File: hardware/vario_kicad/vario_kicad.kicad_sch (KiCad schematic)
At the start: 58 parts, among them P1 USB_C_Plug_USB2.0, U2 BME280, U3 W25Q128JVS, U4 STM32L072CBTx

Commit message: updates;
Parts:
- added Q1: PMOS, symbol Simulation_SPICE:PMOS
- added Q2: NMOS, symbol Simulation_SPICE:NMOS
- added R25: 22k, symbol Device:R
- added R26, R27: 100k, symbol Device:R
- BT1: footprint (none) -> symbol_lib:lipo_footprint; now not fitted
- R22: value 10mR -> 10k
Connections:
- net AUDIO_AMP_ENABLE: now also R16.1; no longer R16.2
- net GND: now also BT1.2 (-), R16.2, Q2.3 (S), R25.2, R27.2; no longer R22.2
- net VBATT: now also Q1.3 (S), R26.2; no longer R16.1
- net ADC_IN3: now reaches U4.13 (PA3)
- net ADC_IN3: now also R22.2, R25.1
- net BP_DIVIDER_ENABLE: now reaches U4.39 (PB3)
- net BP_DIVIDER_ENABLE: now also Q2.2 (G), R27.1
- net VBATT_SW: now reaches R22.1
- net VBATT_SW: now also Q1.1 (D); no longer BT1.2 (-)
- new net: Q1.2 (G), Q2.1 (D), R26.1
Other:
- note added: "#TODO add 3 push buttons"
- note added: "#TODO should it be vbatt or vbatt_sw"
- note added: "Battery charge and regulator"
- note added: "Battery level measuring circuit"
- note added: "I_charge = 100mA"
- note added: "Max V_BATT voltage 4.3V max adc voltage 2.95V"
- note added: "audio amp disabled by default"
- note added: "~0.1uA in sleep mode"
- note added: "~1uA in power-down"
- note removed: "TODO add a current sense amplifier"
- moved on the sheet: C11, C12, C13, D4, R23, R24, TP7, TP8, U5, U6

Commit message: add push button switches
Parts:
- added J1: ~, symbol_lib:SWD_programming, symbol New_Library:SWD_PROGRAMMING
- R22: value 10k -> 100k
- R25: value 22k -> 220k
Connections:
- net GND: now also J1.4 (GND)
- net MEM_CS_ALT: now also U4.40 (PB4); no longer U4.12 (PA2)
- net SWCLK: now also J1.3 (SWD_CLK)
- net SWDIO: now also J1.2 (SWD_TDIO)
- net VBATT: no longer C5.1, C9.1, U1.6 (VCC)
- net VBATT_SW: now also C5.1, C9.1, U1.6 (VCC)
- net VCC: now also J1.1 (3V3)
- net SW1: now reaches U4.41 (PB5)
- net SW3: now reaches U4.42 (PB6)
- net BP_DIVIDER_ENABLE renamed VBATT_SW_EN
- net TIM2_CH1 renamed TIM2_CH3
- net TIM2_CH3: now also U4.12 (PA2); no longer U4.10 (PA0)
- new net WKUP1: U4.10 (PA0)
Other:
- added sheet switch1 (myswitch.kicad_sch)
- added sheet switch2 (myswitch.kicad_sch)
- added sheet switch3 (myswitch.kicad_sch)
- note removed: "#TODO add 3 push buttons"
- note removed: "#TODO should it be vbatt or vbatt_sw"
- note removed: "Battery level measuring circuit"

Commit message: minor updates
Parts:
- removed L1: 10uH, symbol Device:L
- removed U6: ~, Package_TO_SOT_SMD:SOT-23, symbol New_Library:____XC6206P332MR-G
- added U6: ~, Package_TO_SOT_SMD:SOT-23, symbol New_Library:XC6206P332MR-G
- BT1: now fitted
- C10: value 1uF -> 10nF
- R21: value 330R -> 680R
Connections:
- net AUDIO_AMP_ENABLE: now also R16.2; no longer R16.1
- net GND: now also U6.1 (VSS); no longer R16.2
- net VBATT: now also U6.2 (VOUT)
- net VBATT_SW: now also R16.1
- net VCC: now also U6.2 (VOUT)
- net at R21.1: now also C10.1, R20.2
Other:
- note added: "audio amp enabled by default"
- note added: "f_cutoff = 23.4 kHz"
- note removed: "audio amp disabled by default"
- moved on the sheet: R21

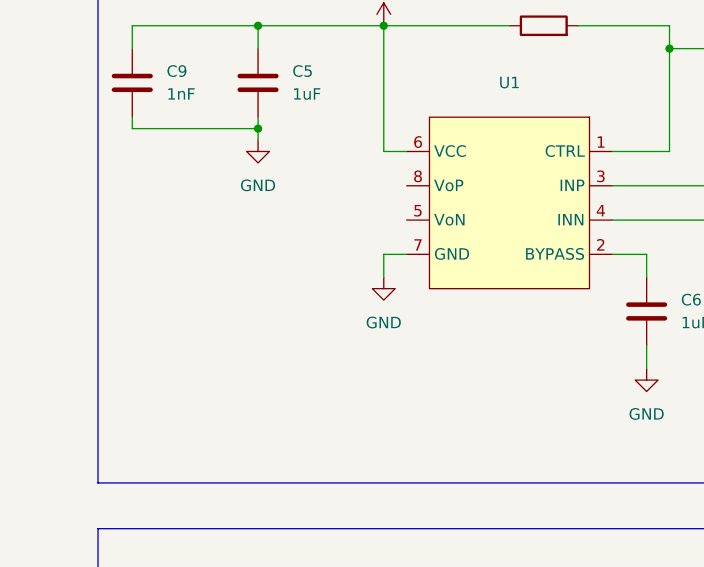
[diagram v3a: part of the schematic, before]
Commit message: update some component footprints
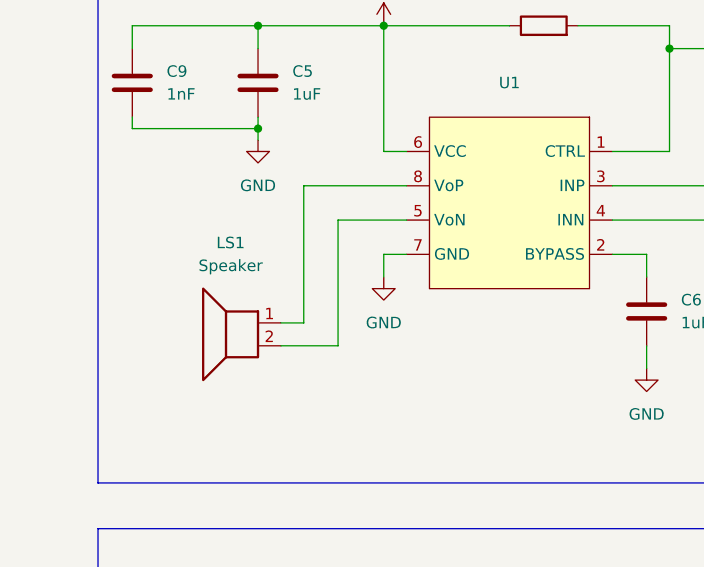
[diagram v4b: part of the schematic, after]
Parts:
- added LS1: Speaker, symbol_lib:speaker_footprint, symbol Device:Speaker
- C1, C10, C11, C12, C13, C2, C3, C4, C5, C6, C7, C8, C9: footprint (none) -> Capacitor_SMD:C_0603_1608Metric
- D1, D2, D3, D4: footprint (none) -> LED_SMD:LED_0603_1608Metric_Pad1.05x0.95mm_HandSolder
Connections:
- net at U1.5 (VoN): now also LS1.2
- net at U1.8 (VoP): now also LS1.1
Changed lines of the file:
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@@
 	(wire
 		(pts
+			(xy 45.72 176.53) (xy 57.15 176.53)
+		)
+		(stroke
+			(width 0)
+			(type default)
+		)
+	)
+	(wire
+		(pts
 			(xy 40.64 135.89) (xy 67.31 135.89)
 		)
@@
 	(wire
 		(pts
+			(xy 57.15 180.34) (xy 49.53 180.34)
+		)
+		(stroke
+			(width 0)
+			(type default)
+		)
+	)
+	(wire
+		(pts
 			(xy 90.17 41.91) (xy 90.17 46.99)
 		)
@@
 	(wire
 		(pts
+			(xy 49.53 180.34) (xy 49.53 194.31)
+		)
+		(stroke
+			(width 0)
+			(type default)
+		)
+	)
+	(wire
+		(pts
 			(xy 45.72 26.67) (xy 45.72 29.21)
 		)
@@
 	(wire
 		(pts
+			(xy 49.53 194.31) (xy 43.18 194.31)
+		)
+		(stroke
+			(width 0)
+			(type default)
+		)
+	)
+	(wire
+		(pts
 			(xy 40.64 168.91) (xy 40.64 170.18)
 		)
@@
 	(wire
 		(pts
+			(xy 45.72 191.77) (xy 45.72 176.53)
+		)
+		(stroke
+			(width 0)
+			(type default)
+		)
+	)
+	(wire
+		(pts
 			(xy 388.62 236.22) (xy 388.62 238.76)
 		)
@@
 	(wire
 		(pts
+			(xy 43.18 191.77) (xy 45.72 191.77)
+		)
+		(stroke
+			(width 0)
+			(type default)
+		)
+	)
+	(wire
+		(pts
 			(xy 254 133.35) (xy 265.43 133.35)
 		)
@@
 			)
 		)
-		(property "Footprint" ""
+		(property "Footprint" "LED_SMD:LED_0603_1608Metric_Pad1.05x0.95mm_HandSolder"
 			(at 373.38 220.98 0)
 			(effects
@@
 			)
 		)
-		(property "Footprint" ""
+		(property "Footprint" "LED_SMD:LED_0603_1608Metric_Pad1.05x0.95mm_HandSolder"
 			(at 388.62 220.98 0)
 			(effects
@@
 			)
 		)
-		(property "Footprint" ""
+		(property "Footprint" "Capacitor_SMD:C_0603_1608Metric"
 			(at 27.6352 168.91 0)
 			(effects
@@
 			)
 		)
-		(property "Footprint" ""
+		(property "Footprint" "Capacitor_SMD:C_0603_1608Metric"
 			(at 274.0152 238.76 0)
 			(effects
@@
 			)
 		)
-		(property "Footprint" ""
+		(property "Footprint" "Capacitor_SMD:C_0603_1608Metric"
 			(at 41.6052 168.91 0)
 			(effects
@@
 			)
 		)
-		(property "Footprint" ""
+		(property "Footprint" "Capacitor_SMD:C_0603_1608Metric"
 			(at 219.4052 113.03 0)
 			(effects
@@
 			)
 		)
-		(property "Footprint" ""
+		(property "Footprint" "Capacitor_SMD:C_0603_1608Metric"
 			(at 36.5252 236.22 0)
 			(effects
@@
 			)
 		)
-		(property "Footprint" ""
+		(property "Footprint" "Capacitor_SMD:C_0603_1608Metric"
 			(at 121.6152 57.15 0)
 			(effects
@@
 			)
 		)
-		(property "Footprint" ""
+		(property "Footprint" "LED_SMD:LED_0603_1608Metric_Pad1.05x0.95mm_HandSolder"
 			(at 356.87 220.98 0)
 			(effects
@@
 			)
 		)
-		(property "Footprint" ""
+		(property "Footprint" "Capacitor_SMD:C_0603_1608Metric"
 			(at 21.2852 38.1 0)
 			(effects
@@
 			)
 		)
-		(property "Datasheet" "https://ngspice.sourceforge.io/docs/ngspice-html-manual/manual.xhtml#cha_MOSFETs"
+		(property "Datasheet" ""
 			(at 46.99 91.44 0)
 			(effects
@@
 			)
 		)
-		(property "Datasheet" "https://www.usb.org/sites/default/files/documents/usb_type-c.zip"
+		(property "Datasheet" ""
 			(at 383.54 133.35 0)
 			(effects
@@
 			)
 		)
-		(property "Footprint" ""
+		(property "Footprint" "Capacitor_SMD:C_0603_1608Metric"
 			(at 50.4952 236.22 0)
 			(effects
@@
 			)
 		)
-		(property "Footprint" ""
+		(property "Footprint" "Capacitor_SMD:C_0603_1608Metric"
 			(at 142.24 184.4548 0)
 			(effects
@@
 			)
 		)
-		(property "Footprint" ""
+		(property "Footprint" "Capacitor_SMD:C_0603_1608Metric"
 			(at 168.6052 189.23 0)
 			(effects
@@
 			)
 		)
-		(property "Footprint" ""
+		(property "Footprint" "Capacitor_SMD:C_0603_1608Metric"
 			(at 142.24 170.4848 0)
 			(effects
@@
 			)
 		)
-		(property "Datasheet" "https://ngspice.sourceforge.io/docs/ngspice-html-manual/manual.xhtml#cha_MOSFETs"
+		(property "Datasheet" ""
 			(at 31.75 133.35 0)
 			(effects
@@
 			)
 		)
-		(property "Footprint" ""
+		(property "Footprint" "LED_SMD:LED_0603_1608Metric_Pad1.05x0.95mm_HandSolder"
 			(at 33.02 39.37 0)
 			(effects
@@
 			)
 		)
-		(property "Footprint" ""
+		(property "Footprint" "Capacitor_SMD:C_0603_1608Metric"
 			(at 167.3352 57.15 0)
 			(effects
@@
 	)
 	(symbol
+		(lib_id "Device:Speaker")
+		(at 38.1 191.77 0)
+		(mirror y)
+		(unit 1)
+		(exclude_from_sim no)
+		(in_bom yes)
+		(on_board yes)
+		(dnp no)
+		(fields_autoplaced yes)
+		(property "Reference" "LS1"
+			(at 37.592 182.88 0)
+			(effects
+				(font
+					(size 1.27 1.27)
+				)
+			)
+		)
+		(property "Value" "Speaker"
+			(at 37.592 185.42 0)
+			(effects
+				(font
+					(size 1.27 1.27)
+				)
+			)
+		)
+		(property "Footprint" "symbol_lib:speaker_footprint"
+			(at 38.1 196.85 0)
+			(effects
+				(font
+					(size 1.27 1.27)
+				)
+				(hide yes)
+			)
+		)
+		(property "Datasheet" "https://www.lcsc.com/product-detail/Speakers_INGHAi-GSPK2307P-8R1W_C530531.html"
+			(at 38.354 193.04 0)
+			(effects
+				(font
+					(size 1.27 1.27)
+				)
+				(hide yes)
+			)
+		)
+		(property "Description" "Speaker"
+			(at 38.1 191.77 0)
+			(effects
+				(font
+					(size 1.27 1.27)
+				)
+				(hide yes)
+			)
+		)
+		(pin "1"
+		)
+		(pin "2"
+		)
+		(instances
+			(project ""
+				(path "/50389aff-b244-451e-8e3a-c5addd2215e1"
+					(reference "LS1")
+					(unit 1)
+				)
+			)
+		)
+	)
+	(symbol
 		(lib_id "Device:R")
 		(at 72.39 158.75 90)
@@
 			)
 		)
-		(property "Footprint" ""
+		(property "Footprint" "Capacitor_SMD:C_0603_1608Metric"
 			(at 84.7852 194.31 0)
 			(effects

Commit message: move external components to separate sheets
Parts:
- removed BT1: Battery_Cell, symbol_lib:lipo_footprint, symbol Device:Battery_Cell
- removed C1, C2, C3, C7, C8: 100nF, Capacitor_SMD:C_0603_1608Metric, symbol Device:C
- removed C10: 10nF, Capacitor_SMD:C_0603_1608Metric, symbol Device:C
- removed C11, C12, C13, C5, C6: 1uF, Capacitor_SMD:C_0603_1608Metric, symbol Device:C
- removed C9: 1nF, Capacitor_SMD:C_0603_1608Metric, symbol Device:C
- removed D1, D2, D3, D4: LED, LED_SMD:LED_0603_1608Metric_Pad1.05x0.95mm_HandSolder, symbol Device:LED
- removed LS1: Speaker, symbol_lib:speaker_footprint, symbol Device:Speaker
- removed Q1: PMOS, symbol Simulation_SPICE:PMOS
- removed Q2: NMOS, symbol Simulation_SPICE:NMOS
- removed R1, R2: 4k7, symbol Device:R
- removed R10, R11, R24, R3: 10k, symbol Device:R
- removed R12, R13, R14: 1k, symbol Device:R
- removed R16, R17, R18, R22, R26, R27: 100k, symbol Device:R
- removed R19, R20, R5, R6, R7, R8, R9: 0R, symbol Device:R
- removed R21: 680R, symbol Device:R
- removed R23: 330R, symbol Device:R
- removed R25: 220k, symbol Device:R
- removed TP1, TP2: ~, symbol Connector:TestPoint
- removed TP7, TP8: TestPoint, symbol Connector:TestPoint
- removed U1: ~, Package_SO:MSOP-8-1EP_3x3mm_P0.65mm_EP1.73x1.85mm, symbol New_Library:NS4150B
- removed U2: BME280, Package_LGA:Bosch_LGA-8_2.5x2.5mm_P0.65mm_ClockwisePinNumbering, symbol Sensor:BME280
- removed U3: W25Q128JVS, Package_SO:SOIC-8_5.23x5.23mm_P1.27mm, symbol Memory_Flash:W25Q128JVS
- removed U5: ~, Package_TO_SOT_SMD:SOT-23-5, symbol New_Library:TP4054
- removed U6: ~, Package_TO_SOT_SMD:SOT-23, symbol New_Library:XC6206P332MR-G
- P1: footprint (none) -> symbol_lib:my_usbc
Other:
- added sheet audio_amp (audio_amp.kicad_sch)
- added sheet bme280 (bme280.kicad_sch)
- added sheet leds (leds.kicad_sch)
- added sheet memory (memory.kicad_sch)
- added sheet power (power.kicad_sch)
- note removed: "Battery charge and regulator"
- note removed: "I_charge = 100mA"
- note removed: "Max V_BATT voltage 4.3V max adc voltage 2.95V"
- note removed: "SDO = high => i2c address = 0x77"
- note removed: "audio amp enabled by default"
- note removed: "f_cutoff = 23.4 kHz"
- note removed: "gain settings resistors"
- note removed: "~0.1uA in sleep mode"
- note removed: "~1uA in power-down"
- moved on the sheet: C4, J1, P1, R15, R4, TP3, TP4, TP5, TP6, U4

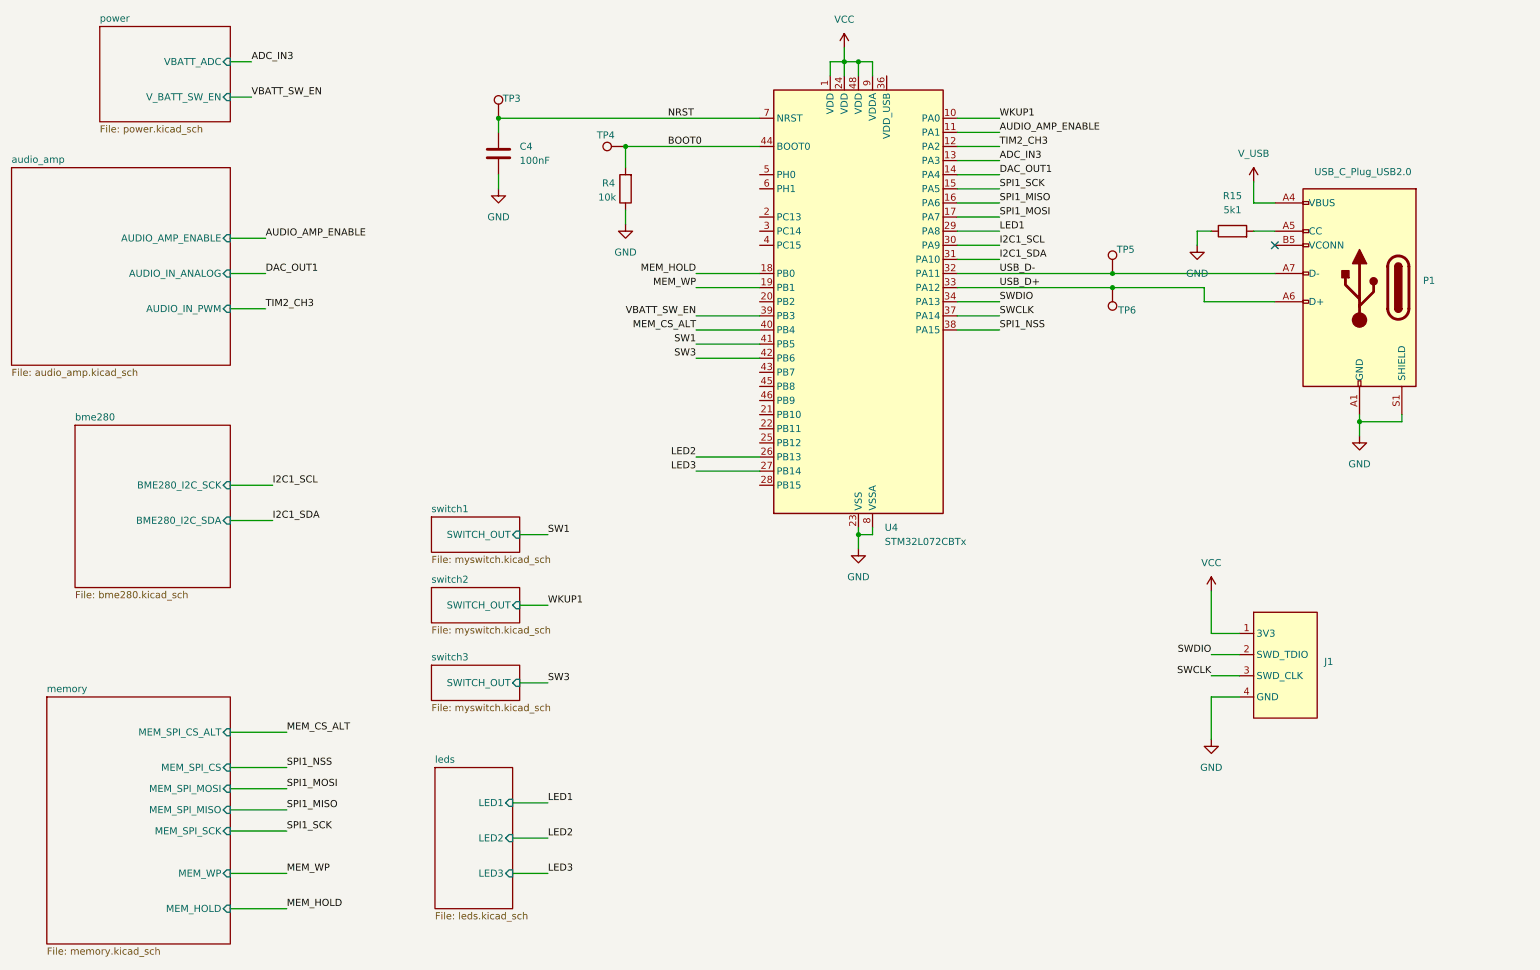
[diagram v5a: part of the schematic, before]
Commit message: all components in hier sheets
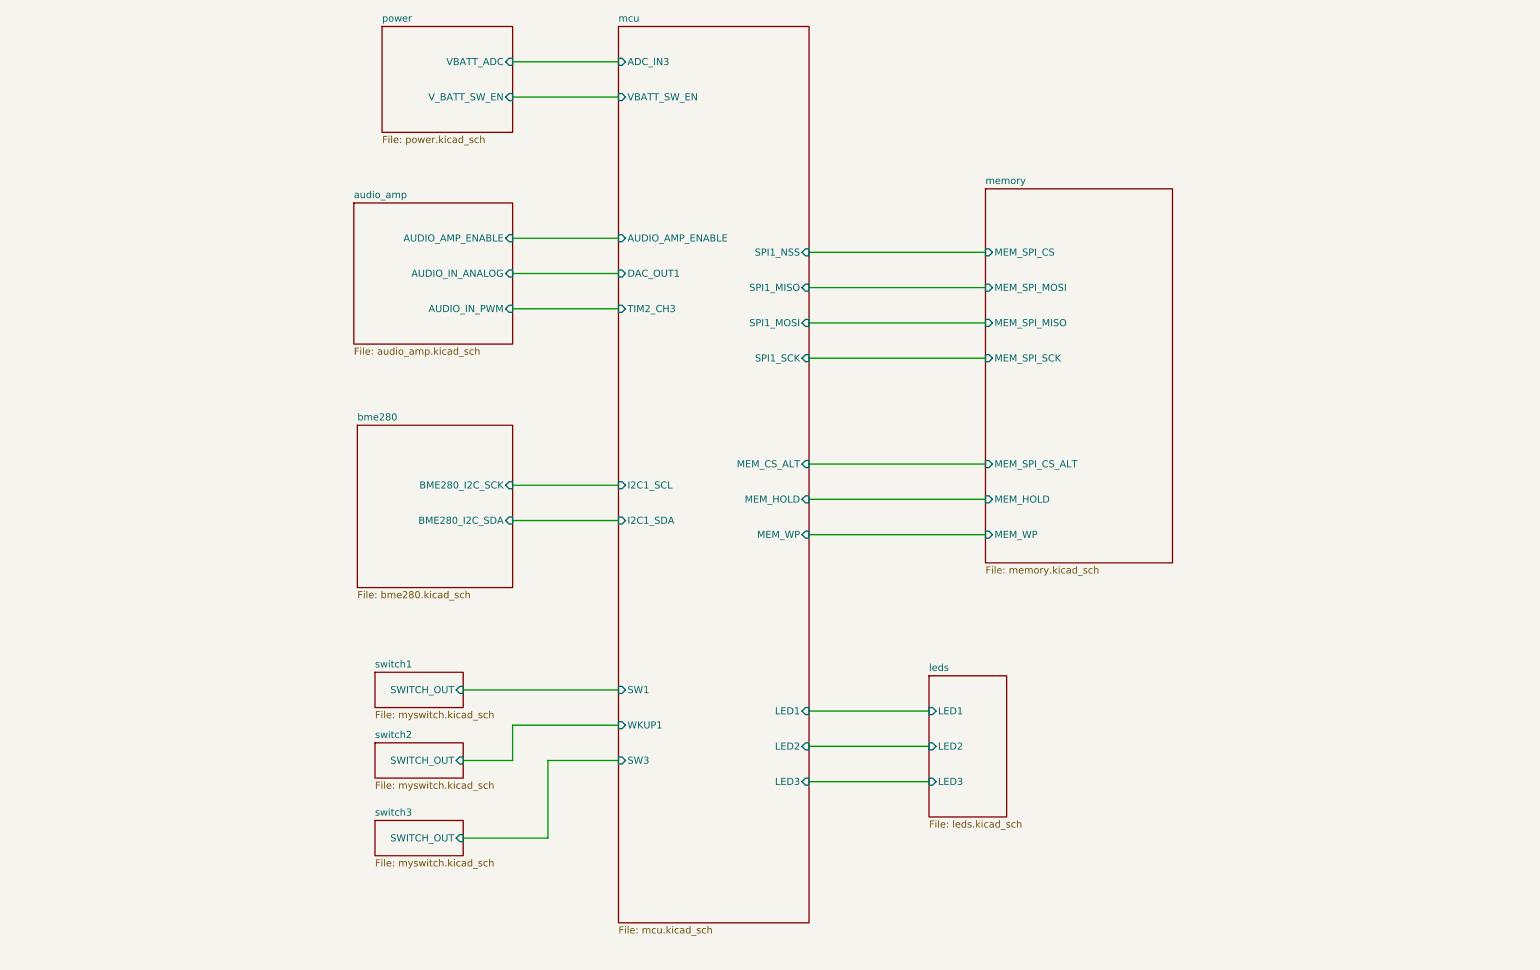
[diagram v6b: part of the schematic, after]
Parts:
- removed C4: 100nF, Capacitor_SMD:C_0603_1608Metric, symbol Device:C
- removed J1: ~, symbol_lib:SWD_programming, symbol New_Library:SWD_PROGRAMMING
- removed P1: USB_C_Plug_USB2.0, symbol_lib:my_usbc, symbol Connector:USB_C_Plug_USB2.0
- removed R15: 5k1, symbol Device:R
- removed R4: 10k, symbol Device:R
- removed TP3, TP4: ~, symbol Connector:TestPoint
- removed TP5, TP6: TestPoint, symbol Connector:TestPoint
- removed U4: STM32L072CBTx, Package_QFP:LQFP-48_7x7mm_P0.5mm, symbol MCU_ST_STM32L0:STM32L072CBTx
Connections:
- no-connect marks 2 -> 1
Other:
- added sheet mcu (mcu.kicad_sch)

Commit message: start layout
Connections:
- no-connect marks 1 -> 0
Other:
- sheet mcu ports: added USB_D+, USB_D-; removed none
- sheet power ports: added USB_D+, USB_D-; removed none
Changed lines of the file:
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@@
 	(generator_version "8.0")
 	(paper "A4")
-	(no_connect
-		(at 342.9 76.2)
+	(wire
+		(pts
+			(xy 124.46 46.99) (xy 124.46 44.45)
+		)
+		(stroke
+			(width 0)
+			(type default)
+		)
 	)
 	(wire
@@
 	(wire
 		(pts
+			(xy 82.55 25.4) (xy 69.85 25.4)
+		)
+		(stroke
+			(width 0)
+			(type default)
+		)
+	)
+	(wire
+		(pts
+			(xy 69.85 25.4) (xy 69.85 46.99)
+		)
+		(stroke
+			(width 0)
+			(type default)
+		)
+	)
+	(wire
+		(pts
+			(xy 69.85 46.99) (xy 124.46 46.99)
+		)
+		(stroke
+			(width 0)
+			(type default)
+		)
+	)
+	(wire
+		(pts
+			(xy 76.2 31.75) (xy 82.55 31.75)
+		)
+		(stroke
+			(width 0)
+			(type default)
+		)
+	)
+	(wire
+		(pts
 			(xy 114.3 25.4) (xy 133.35 25.4)
 		)
@@
 	(wire
 		(pts
+			(xy 116.84 43.18) (xy 76.2 43.18)
+		)
+		(stroke
+			(width 0)
+			(type default)
+		)
+	)
+	(wire
+		(pts
 			(xy 167.64 142.24) (xy 189.23 142.24)
 		)
@@
 	(wire
 		(pts
+			(xy 133.35 38.1) (xy 116.84 38.1)
+		)
+		(stroke
+			(width 0)
+			(type default)
+		)
+	)
+	(wire
+		(pts
 			(xy 120.65 151.13) (xy 133.35 151.13)
 		)
@@
 	(wire
 		(pts
+			(xy 76.2 43.18) (xy 76.2 31.75)
+		)
+		(stroke
+			(width 0)
+			(type default)
+		)
+	)
+	(wire
+		(pts
+			(xy 124.46 44.45) (xy 133.35 44.45)
+		)
+		(stroke
+			(width 0)
+			(type default)
+		)
+	)
+	(wire
+		(pts
 			(xy 105.41 151.13) (xy 114.3 151.13)
 		)
@@
 		(pts
 			(xy 167.64 66.04) (xy 199.39 66.04)
+		)
+		(stroke
+			(width 0)
+			(type default)
+		)
+	)
+	(wire
+		(pts
+			(xy 116.84 38.1) (xy 116.84 43.18)
 		)
 		(stroke
@@
 	)
 	(sheet
-		(at 90.805 19.05)
-		(size 23.495 19.05)
+		(at 82.55 19.05)
+		(size 31.75 19.05)
 		(fields_autoplaced yes)
 		(stroke
@@
 		)
 		(property "Sheetname" "power"
-			(at 90.805 18.3384 0)
+			(at 82.55 18.3384 0)
 			(effects
 				(font
@@
 		)
 		(property "Sheetfile" "power.kicad_sch"
-			(at 90.805 38.6846 0)
+			(at 82.55 38.6846 0)
 			(effects
 				(font
@@
 				)
 				(justify right)
+			)
+		)
+		(pin "USB_D+" input
+			(at 82.55 25.4 180)
+			(effects
+				(font
+					(size 1.27 1.27)
+				)
+				(justify left)
+			)
+		)
+		(pin "USB_D-" input
+			(at 82.55 31.75 180)
+			(effects
+				(font
+					(size 1.27 1.27)
+				)
+				(justify left)
 			)
 		)
@@
 			)
 		)
+		(pin "USB_D-" input
+			(at 133.35 38.1 180)
+			(effects
+				(font
+					(size 1.27 1.27)
+				)
+				(justify left)
+			)
+		)
+		(pin "USB_D+" input
+			(at 133.35 44.45 180)
+			(effects
+				(font
+					(size 1.27 1.27)
+				)
+				(justify left)
+			)
+		)
